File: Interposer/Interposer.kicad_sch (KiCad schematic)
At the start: 15 parts, among them J1 Cis_Electrode_In, J10 Trans_Electrode_Out, J11 Trans_Electrode_In, J2 Cis_Electrode_Out, P1 Port_Cis_In_30deg, P2 Port_Cis_Out_330deg, P3 Port_Trans_In_210deg, P4 Port_Trans_Out_150deg

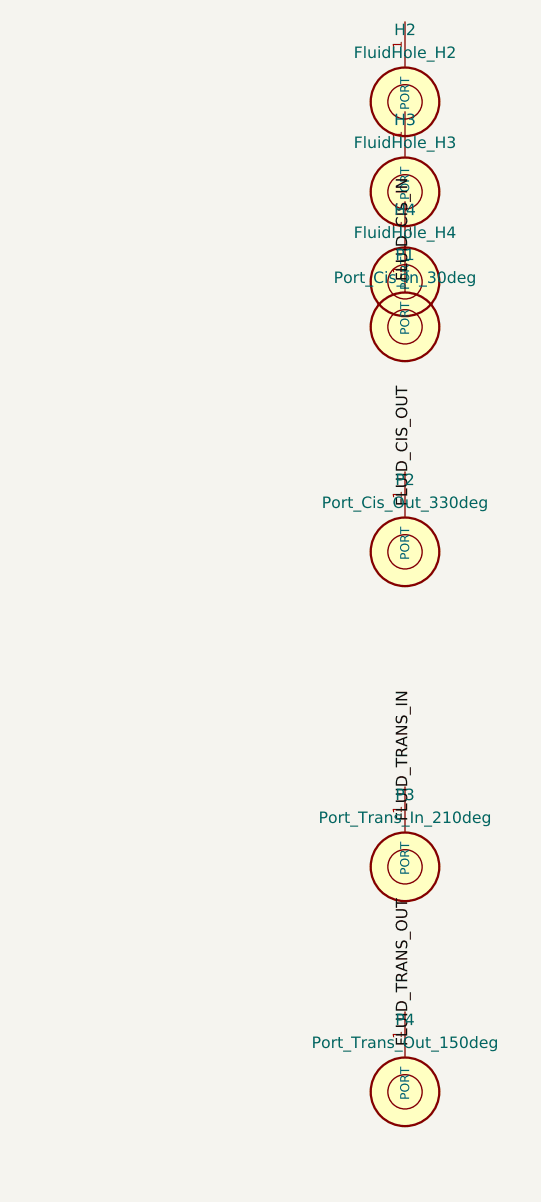
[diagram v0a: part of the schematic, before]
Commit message: Fix interposer fluid channel routing and update default footprints
Co-authored-by: google-labs-jules[bot] <161369871+google-labs-jules[bot]@users.noreply.github.com>
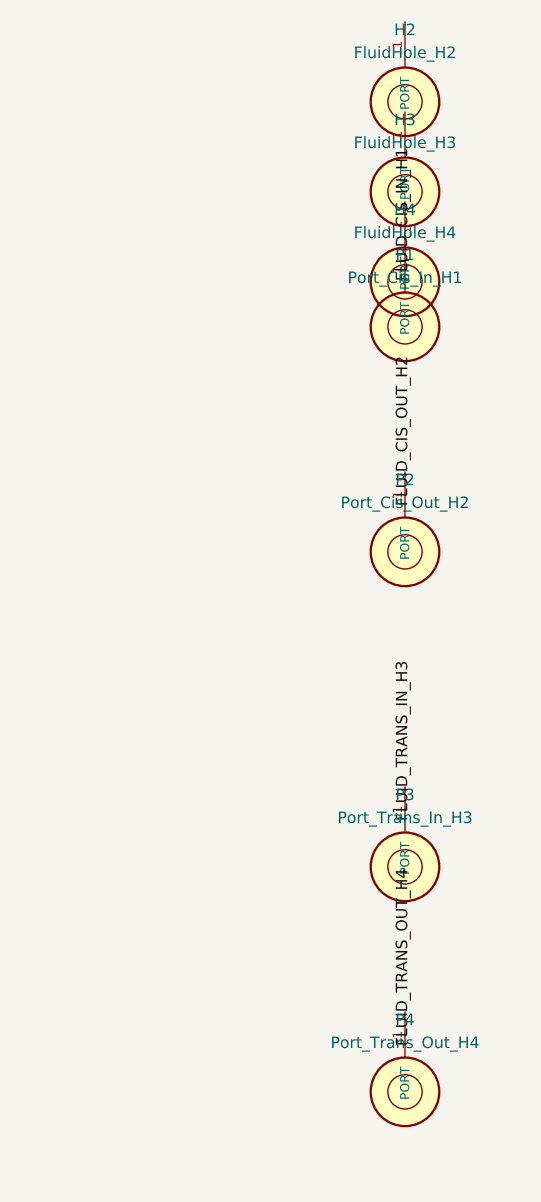
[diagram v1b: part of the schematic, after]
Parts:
- P1: value Port_Cis_In_30deg -> Port_Cis_In_H1
- P2: value Port_Cis_Out_330deg -> Port_Cis_Out_H2
- P3: value Port_Trans_In_210deg -> Port_Trans_In_H3
- P4: value Port_Trans_Out_150deg -> Port_Trans_Out_H4
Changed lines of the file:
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@@
 		(fields_autoplaced yes)
 		(property "Reference" "P1" (at 320.0 37.0 0) (effects (font (size 1.27 1.27))))
-		(property "Value" "Port_Cis_In_30deg" (at 320.0 39.54 0) (effects (font (size 1.27 1.27))))
+		(property "Value" "Port_Cis_In_H1" (at 320.0 39.54 0) (effects (font (size 1.27 1.27))))
 		(property "Footprint" "" (at 320.0 45.0 0) (hide yes) (effects (font (size 1.27 1.27))))
 		(property "Datasheet" "~" (at 320.0 45.0 0) (hide yes) (effects (font (size 1.27 1.27))))
-		(property "Description" "D=2.0mm Microfluidic Pass-Through Port (Cis Inlet, 30 deg, r=20mm)" (at 320.0 45.0 0) (hide yes) (effects (font (size 1.27 1.27))))
+		(property "Description" "D=2.1mm Microfluidic Pass-Through Port (Cis Inlet H1)" (at 320.0 45.0 0) (hide yes) (effects (font (size 1.27 1.27))))
 		(pin "1")
 	)
@@
 		(fields_autoplaced yes)
 		(property "Reference" "P2" (at 320.0 62.0 0) (effects (font (size 1.27 1.27))))
-		(property "Value" "Port_Cis_Out_330deg" (at 320.0 64.54 0) (effects (font (size 1.27 1.27))))
+		(property "Value" "Port_Cis_Out_H2" (at 320.0 64.54 0) (effects (font (size 1.27 1.27))))
 		(property "Footprint" "" (at 320.0 70.0 0) (hide yes) (effects (font (size 1.27 1.27))))
 		(property "Datasheet" "~" (at 320.0 70.0 0) (hide yes) (effects (font (size 1.27 1.27))))
-		(property "Description" "D=2.0mm Microfluidic Pass-Through Port (Cis Outlet, 330 deg, r=20mm)" (at 320.0 70.0 0) (hide yes) (effects (font (size 1.27 1.27))))
+		(property "Description" "D=2.1mm Microfluidic Pass-Through Port (Cis Outlet H2)" (at 320.0 70.0 0) (hide yes) (effects (font (size 1.27 1.27))))
 		(pin "1")
 	)
@@
 		(fields_autoplaced yes)
 		(property "Reference" "P3" (at 320.0 97.0 0) (effects (font (size 1.27 1.27))))
-		(property "Value" "Port_Trans_In_210deg" (at 320.0 99.54 0) (effects (font (size 1.27 1.27))))
+		(property "Value" "Port_Trans_In_H3" (at 320.0 99.54 0) (effects (font (size 1.27 1.27))))
 		(property "Footprint" "" (at 320.0 105.0 0) (hide yes) (effects (font (size 1.27 1.27))))
 		(property "Datasheet" "~" (at 320.0 105.0 0) (hide yes) (effects (font (size 1.27 1.27))))
-		(property "Description" "D=2.0mm Microfluidic Pass-Through Port (Trans Inlet, 210 deg, r=20mm)" (at 320.0 105.0 0) (hide yes) (effects (font (size 1.27 1.27))))
+		(property "Description" "D=2.1mm Microfluidic Pass-Through Port (Trans Inlet H3)" (at 320.0 105.0 0) (hide yes) (effects (font (size 1.27 1.27))))
 		(pin "1")
 	)
@@
 		(fields_autoplaced yes)
 		(property "Reference" "P4" (at 320.0 122.0 0) (effects (font (size 1.27 1.27))))
-		(property "Value" "Port_Trans_Out_150deg" (at 320.0 124.54 0) (effects (font (size 1.27 1.27))))
+		(property "Value" "Port_Trans_Out_H4" (at 320.0 124.54 0) (effects (font (size 1.27 1.27))))
 		(property "Footprint" "" (at 320.0 130.0 0) (hide yes) (effects (font (size 1.27 1.27))))
 		(property "Datasheet" "~" (at 320.0 130.0 0) (hide yes) (effects (font (size 1.27 1.27))))
-		(property "Description" "D=2.0mm Microfluidic Pass-Through Port (Trans Outlet, 150 deg, r=20mm)" (at 320.0 130.0 0) (hide yes) (effects (font (size 1.27 1.27))))
+		(property "Description" "D=2.1mm Microfluidic Pass-Through Port (Trans Outlet H4)" (at 320.0 130.0 0) (hide yes) (effects (font (size 1.27 1.27))))
 		(pin "1")
 	)
@@
 	(label "WEEP_SENSE" (at 158.57 132.54 180) (effects (font (size 1.27 1.27))))
 	(label "GNDA" (at 158.57 127.46 180) (effects (font (size 1.27 1.27))))
-	(label "FLUID_CIS_IN" (at 320.0 39.92 90) (effects (font (size 1.27 1.27))))
-	(label "FLUID_CIS_OUT" (at 320.0 64.92 90) (effects (font (size 1.27 1.27))))
-	(label "FLUID_TRANS_IN" (at 320.0 99.92 90) (effects (font (size 1.27 1.27))))
-	(label "FLUID_TRANS_OUT" (at 320.0 124.92 90) (effects (font (size 1.27 1.27))))
+	(label "FLUID_CIS_IN_H1" (at 320.0 39.92 90) (effects (font (size 1.27 1.27))))
+	(label "FLUID_CIS_OUT_H2" (at 320.0 64.92 90) (effects (font (size 1.27 1.27))))
+	(label "FLUID_TRANS_IN_H3" (at 320.0 99.92 90) (effects (font (size 1.27 1.27))))
+	(label "FLUID_TRANS_OUT_H4" (at 320.0 124.92 90) (effects (font (size 1.27 1.27))))
 )
